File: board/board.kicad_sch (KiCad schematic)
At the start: 4 parts, among them J1 Conn_01x14_Pin, J2 Conn_01x14_Pin, J3 Conn_01x14_Pin, U1 ESP32-WROOM-32

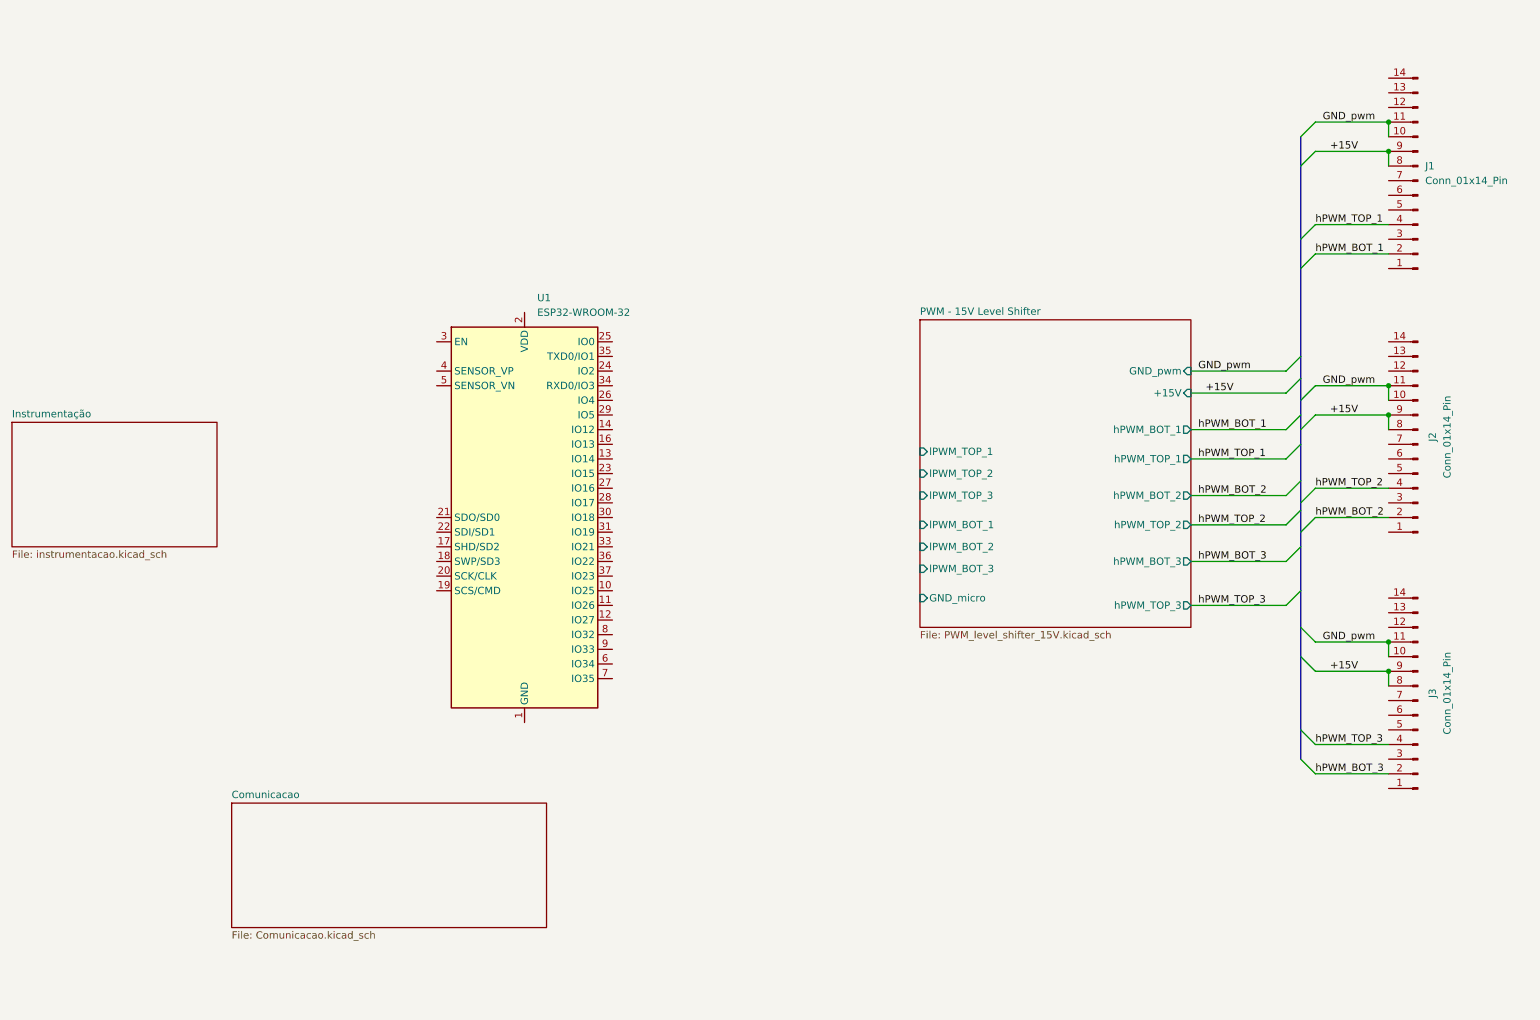
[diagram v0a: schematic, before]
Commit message: Schematic changes: correct micro board and subsystems
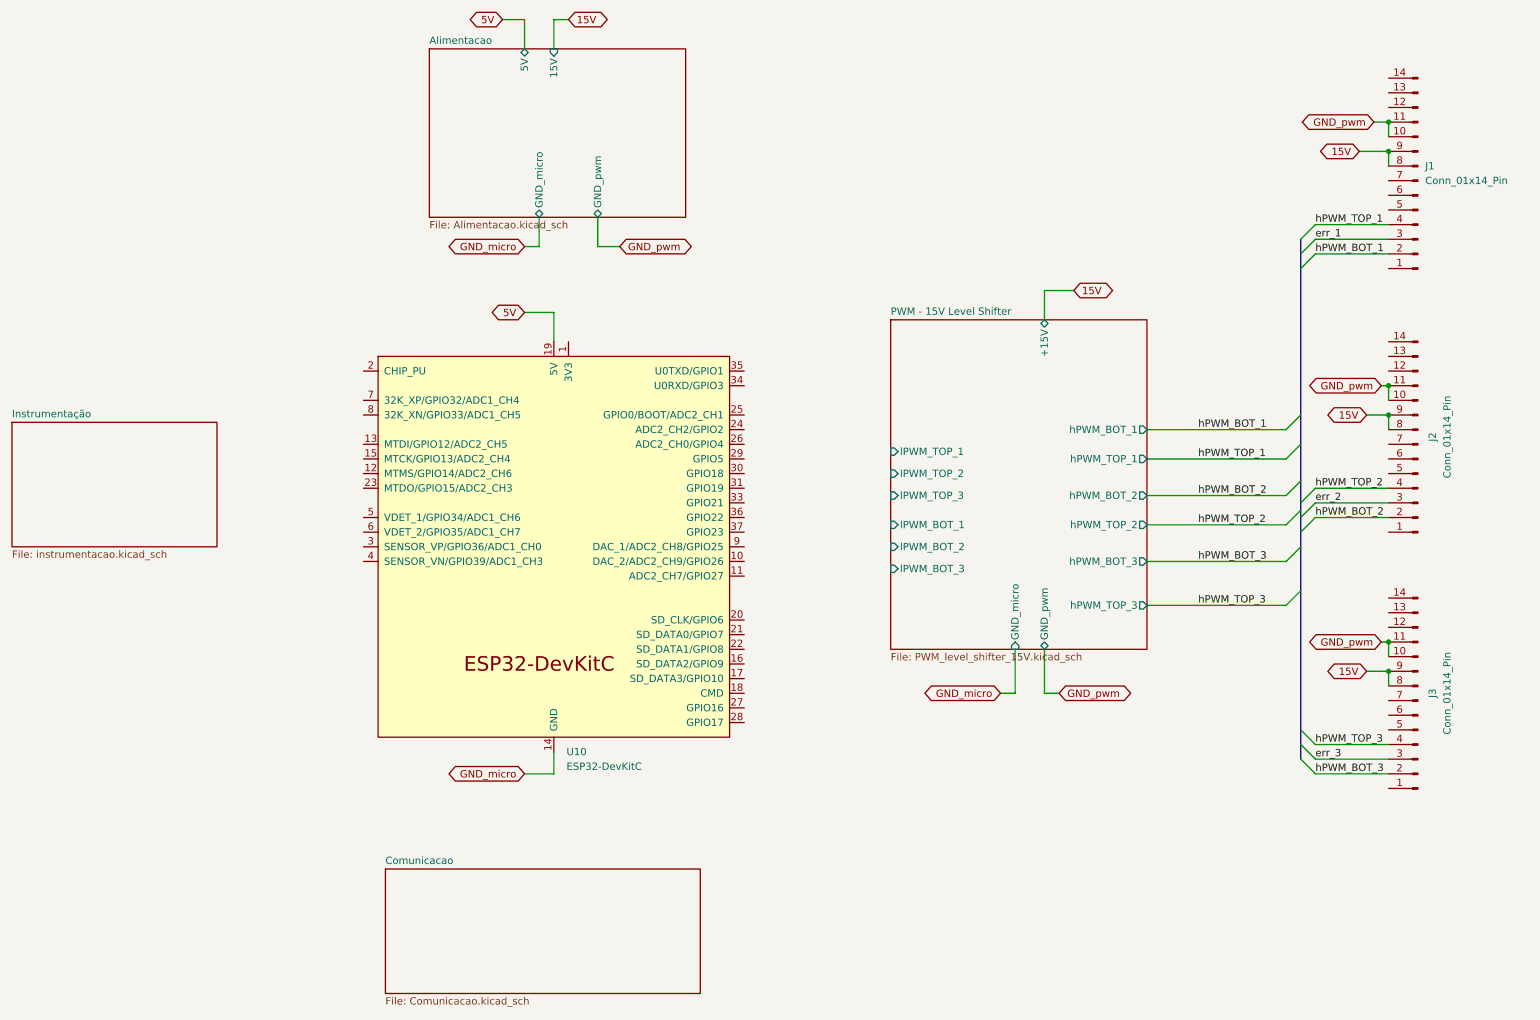
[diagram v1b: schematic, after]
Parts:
- removed U1: ESP32-WROOM-32, RF_Module:ESP32-WROOM-32, symbol RF_Module:ESP32-WROOM-32
- added U10: ESP32-DevKitC, PCM_Espressif:ESP32-DevKitC, symbol PCM_Espressif:ESP32-DevKitC
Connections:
- net err_2: now reaches J2.3 (Pin_3)
- net err_1: now reaches J1.3 (Pin_3)
- net err_3: now reaches J3.3 (Pin_3)
- net +15V renamed 15V
- new net 5V: U10.19 (5V)
- new net GND_micro: U10.14 (GND), U10.32 (GND), U10.38 (GND)
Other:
- added sheet Alimentacao (Alimentacao.kicad_sch)

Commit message: Schematic changes: Complete PWM voltage level shifter
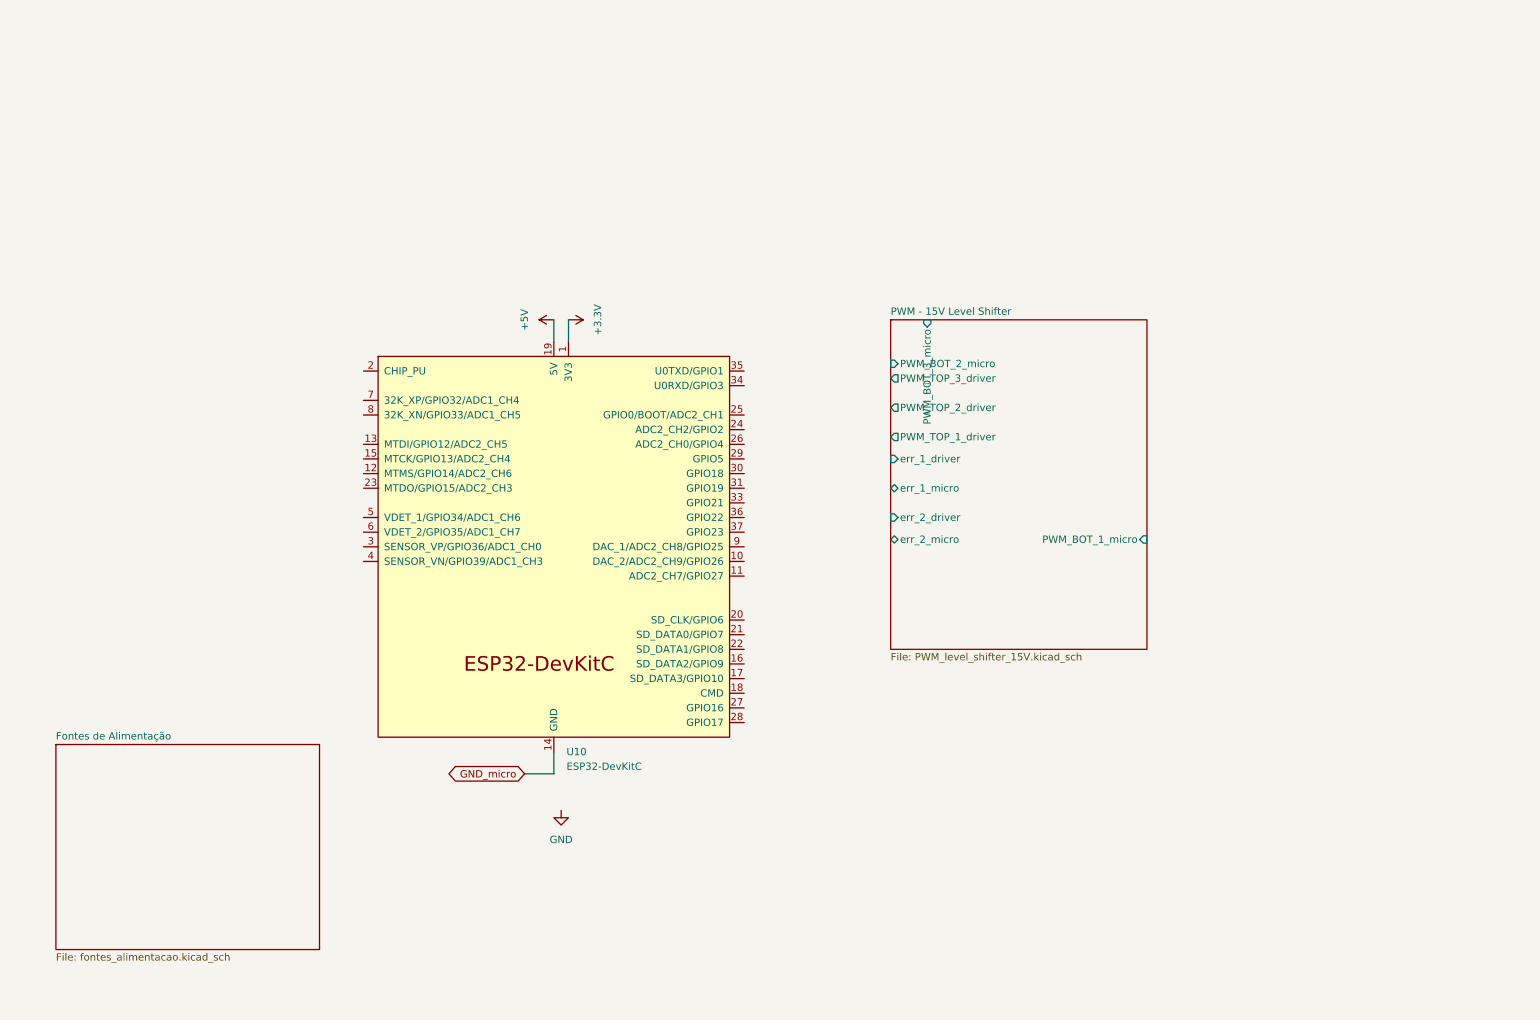
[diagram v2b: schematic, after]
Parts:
- removed J1, J2, J3: Conn_01x14_Pin, symbol Connector:Conn_01x14_Pin
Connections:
- net +3.3V: now reaches U10.1 (3V3)
- net 5V renamed +5V
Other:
- removed sheet Alimentacao
- removed sheet Comunicacao
- removed sheet Instrumentação
- added sheet Fontes de Alimentação (fontes_alimentacao.kicad_sch)
- sheet PWM - 15V Level Shifter ports: added PWM_BOT_1_micro, PWM_BOT_2_micro, PWM_BOT_3_micro, PWM_TOP_1_driver, PWM_TOP_2_driver, PWM_TOP_3_driver, err_1_driver, err_1_micro, err_2_driver, err_2_micro; removed +15V, GND_micro, GND_pwm, hPWM_BOT_1, hPWM_BOT_2, hPWM_BOT_3, hPWM_TOP_1, hPWM_TOP_2, hPWM_TOP_3, lPWM_BOT_1, lPWM_BOT_2, lPWM_BOT_3, lPWM_TOP_1, lPWM_TOP_2, lPWM_TOP_3

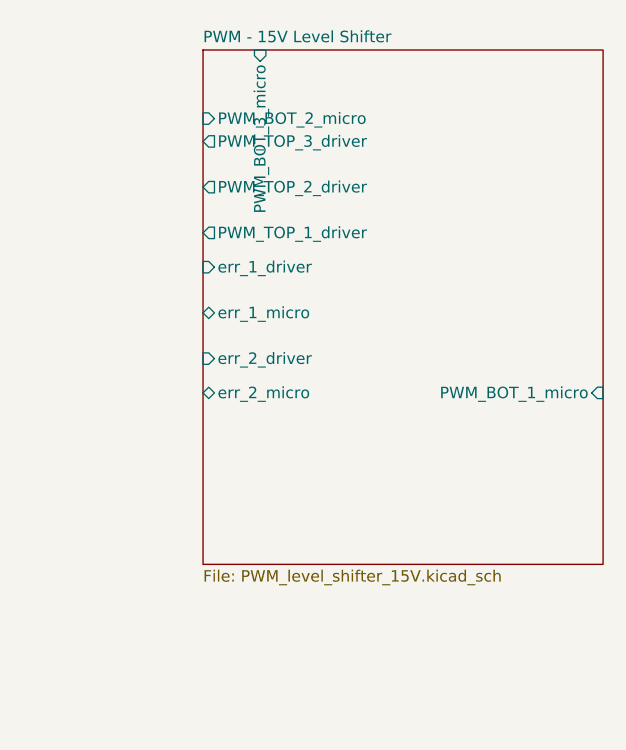
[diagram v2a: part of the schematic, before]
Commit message: Schematic changes: Fix optocoupler output, fix resistor values
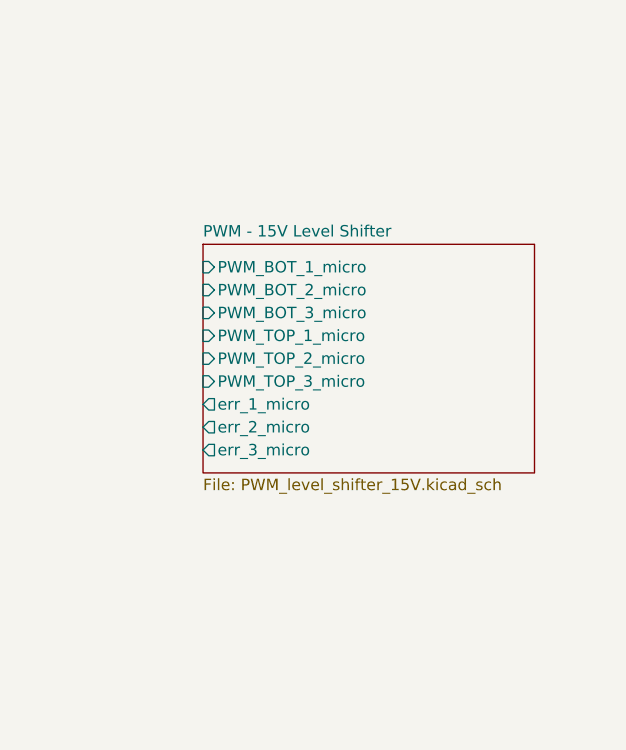
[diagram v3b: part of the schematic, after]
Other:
- sheet PWM - 15V Level Shifter ports: added PWM_TOP_1_micro, PWM_TOP_2_micro, PWM_TOP_3_micro, err_3_micro; removed PWM_TOP_1_driver, PWM_TOP_2_driver, PWM_TOP_3_driver, err_1_driver, err_2_driver
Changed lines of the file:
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@@
 	)
 	(sheet
-		(at 173.99 67.31)
-		(size 44.45 57.15)
+		(at 173.99 88.9)
+		(size 36.83 25.4)
 		(fields_autoplaced yes)
 		(stroke
@@
 		)
 		(property "Sheetname" "PWM - 15V Level Shifter"
-			(at 173.99 66.5984 0)
+			(at 173.99 88.1884 0)
 			(effects
 				(font
@@
 		)
 		(property "Sheetfile" "PWM_level_shifter_15V.kicad_sch"
-			(at 173.99 125.0446 0)
+			(at 173.99 114.8846 0)
 			(effects
 				(font
@@
 			)
 		)
-		(pin "err_2_micro" bidirectional
-			(at 173.99 105.41 180)
+		(property "R_e_pwm" "150"
+			(at 173.99 88.9 0)
+			(effects
+				(font
+					(size 1.27 1.27)
+				)
+				(hide yes)
+			)
+		)
+		(property "R_l_pwm" "1k5"
+			(at 173.99 88.9 0)
+			(effects
+				(font
+					(size 1.27 1.27)
+				)
+				(hide yes)
+			)
+		)
+		(property "C_e_pwm" "C_e_pwm"
+			(at 173.99 88.9 0)
+			(effects
+				(font
+					(size 1.27 1.27)
+				)
+				(hide yes)
+			)
+		)
+		(property "R_e_err" "1k2"
+			(at 173.99 88.9 0)
+			(effects
+				(font
+					(size 1.27 1.27)
+				)
+				(hide yes)
+			)
+		)
+		(property "R_l_err" "470"
+			(at 173.99 88.9 0)
+			(effects
+				(font
+					(size 1.27 1.27)
+				)
+				(hide yes)
+			)
+		)
+		(property "C_e_err" "C_e_err"
+			(at 173.99 88.9 0)
+			(effects
+				(font
+					(size 1.27 1.27)
+				)
+				(hide yes)
+			)
+		)
+		(pin "PWM_BOT_2_micro" input
+			(at 173.99 93.98 180)
 			(effects
 				(font
@@
 			)
 		)
-		(pin "err_2_driver" input
+		(pin "PWM_BOT_3_micro" input
+			(at 173.99 96.52 180)
+			(effects
+				(font
+					(size 1.27 1.27)
+				)
+				(justify left)
+			)
+		)
+		(pin "err_2_micro" output
+			(at 173.99 109.22 180)
+			(effects
+				(font
+					(size 1.27 1.27)
+				)
+				(justify left)
+			)
+		)
+		(pin "PWM_BOT_1_micro" input
+			(at 173.99 91.44 180)
+			(effects
+				(font
+					(size 1.27 1.27)
+				)
+				(justify left)
+			)
+		)
+		(pin "err_1_micro" output
+			(at 173.99 106.68 180)
+			(effects
+				(font
+					(size 1.27 1.27)
+				)
+				(justify left)
+			)
+		)
+		(pin "PWM_TOP_1_micro" input
+			(at 173.99 99.06 180)
+			(effects
+				(font
+					(size 1.27 1.27)
+				)
+				(justify left)
+			)
+		)
+		(pin "PWM_TOP_3_micro" input
+			(at 173.99 104.14 180)
+			(effects
+				(font
+					(size 1.27 1.27)
+				)
+				(justify left)
+			)
+		)
+		(pin "PWM_TOP_2_micro" input
 			(at 173.99 101.6 180)
 			(effects
@@
 			)
 		)
-		(pin "err_1_micro" bidirectional
-			(at 173.99 96.52 180)
+		(pin "err_3_micro" output
+			(at 173.99 111.76 180)
 			(effects
 				(font
@@
 			)
 		)
-		(pin "err_1_driver" input
-			(at 173.99 91.44 180)
-			(effects
-				(font
-					(size 1.27 1.27)
-				)
-				(justify left)
-			)
-		)
-		(pin "PWM_TOP_1_driver" output
-			(at 173.99 87.63 180)
-			(effects
-				(font
-					(size 1.27 1.27)
-				)
-				(justify left)
-			)
-		)
-		(pin "PWM_TOP_2_driver" output
-			(at 173.99 82.55 180)
-			(effects
-				(font
-					(size 1.27 1.27)
-				)
-				(justify left)
-			)
-		)
-		(pin "PWM_TOP_3_driver" output
-			(at 173.99 77.47 180)
-			(effects
-				(font
-					(size 1.27 1.27)
-				)
-				(justify left)
-			)
-		)
-		(pin "PWM_BOT_2_micro" input
-			(at 173.99 74.93 180)
-			(effects
-				(font
-					(size 1.27 1.27)
-				)
-				(justify left)
-			)
-		)
-		(pin "PWM_BOT_3_micro" input
-			(at 180.34 67.31 90)
-			(effects
-				(font
-					(size 1.27 1.27)
-				)
-				(justify right)
-			)
-		)
-		(pin "PWM_BOT_1_micro" input
-			(at 218.44 105.41 0)
-			(effects
-				(font
-					(size 1.27 1.27)
-				)
-				(justify right)
-			)
-		)

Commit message: Schematic changes and board creation
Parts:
- renumbered U10 to U1
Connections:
- net GND_micro is gone; now on net GND: U1.14 (GND), U1.32 (GND), U1.38 (GND)
- net I_read_out: now reaches U1.10 (DAC_2/ADC2_CH9/GPIO26)
- net err_3: now reaches U1.23 (MTDO/GPIO15/ADC2_CH3)
- net PWM_TOP_3: now reaches U1.24 (ADC2_CH2/GPIO2)
- net PWM_BOT_3: now reaches U1.25 (GPIO0/BOOT/ADC2_CH1)
- net err_2: now reaches U1.26 (ADC2_CH0/GPIO4)
- net PWM_TOP_2: now reaches U1.27 (GPIO16)
- net PWM_BOT_2: now reaches U1.28 (GPIO17)
- net err_1: now reaches U1.29 (GPIO5)
- net PWM_TOP_1: now reaches U1.30 (GPIO18)
- net PWM_BOT_1: now reaches U1.31 (GPIO19)
- net V_read_in: now reaches U1.5 (VDET_1/GPIO34/ADC1_CH6)
- net V_read_out: now reaches U1.6 (VDET_2/GPIO35/ADC1_CH7)
- net I_read_L1: now reaches U1.7 (32K_XP/GPIO32/ADC1_CH4)
- net I_read_L2: now reaches U1.8 (32K_XN/GPIO33/ADC1_CH5)
- net I_read_L3: now reaches U1.9 (DAC_1/ADC2_CH8/GPIO25)
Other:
- removed sheet Fontes de Alimentação
- added sheet Adequação Sinais Corrente e Tensão (adequacao_sinais.kicad_sch)
- added sheet Power Connectors (pwr_conn.kicad_sch)
- moved on the sheet: U1
